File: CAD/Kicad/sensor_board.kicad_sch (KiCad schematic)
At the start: 3 parts, among them J2 RJ12_Shielded, U7 BME680, U8 MPU-9250

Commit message: It's super late man
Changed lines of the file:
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@@
+	)
+	(junction
+		(at 41.91 114.3)
+		(diameter 0)
+		(color 0 0 0 0)
 	)
 	(junction
@@
 	)
 	(junction
+		(at 58.42 106.68)
+		(diameter 0)
+		(color 0 0 0 0)
+	)
+	(junction
 		(at 109.22 149.86)
 		(diameter 0)
@@
 	(wire
 		(pts
-			(xy 52.07 106.68) (xy 106.68 106.68)
+			(xy 52.07 106.68) (xy 58.42 106.68)
 		)
 		(stroke
@@
 	(wire
 		(pts
+			(xy 58.42 106.68) (xy 106.68 106.68)
+		)
+		(stroke
+			(width 0)
+			(type default)
+		)
+	)
+	(wire
+		(pts
 			(xy 134.62 97.79) (xy 139.7 97.79)
 		)
@@
 	(wire
 		(pts
+			(xy 41.91 114.3) (xy 41.91 111.76)
+		)
+		(stroke
+			(width 0)
+			(type default)
+		)
+	)
+	(wire
+		(pts
 			(xy 102.87 40.64) (xy 95.25 40.64)
 		)
@@
 	(wire
 		(pts
-			(xy 41.91 149.86) (xy 41.91 111.76)
+			(xy 41.91 149.86) (xy 41.91 114.3)
 		)
 		(stroke
@@
 	(wire
 		(pts
+			(xy 58.42 114.3) (xy 58.42 106.68)
+		)
+		(stroke
+			(width 0)
+			(type default)
+		)
+	)
+	(wire
+		(pts
 			(xy 116.84 78.74) (xy 116.84 85.09)
 		)
 		(stroke
+			(width 0)
+			(type default)
+		)
+	)
+	(wire
+		(pts
+			(xy 41.91 114.3) (xy 58.42 114.3)
+		)
+		(stroke

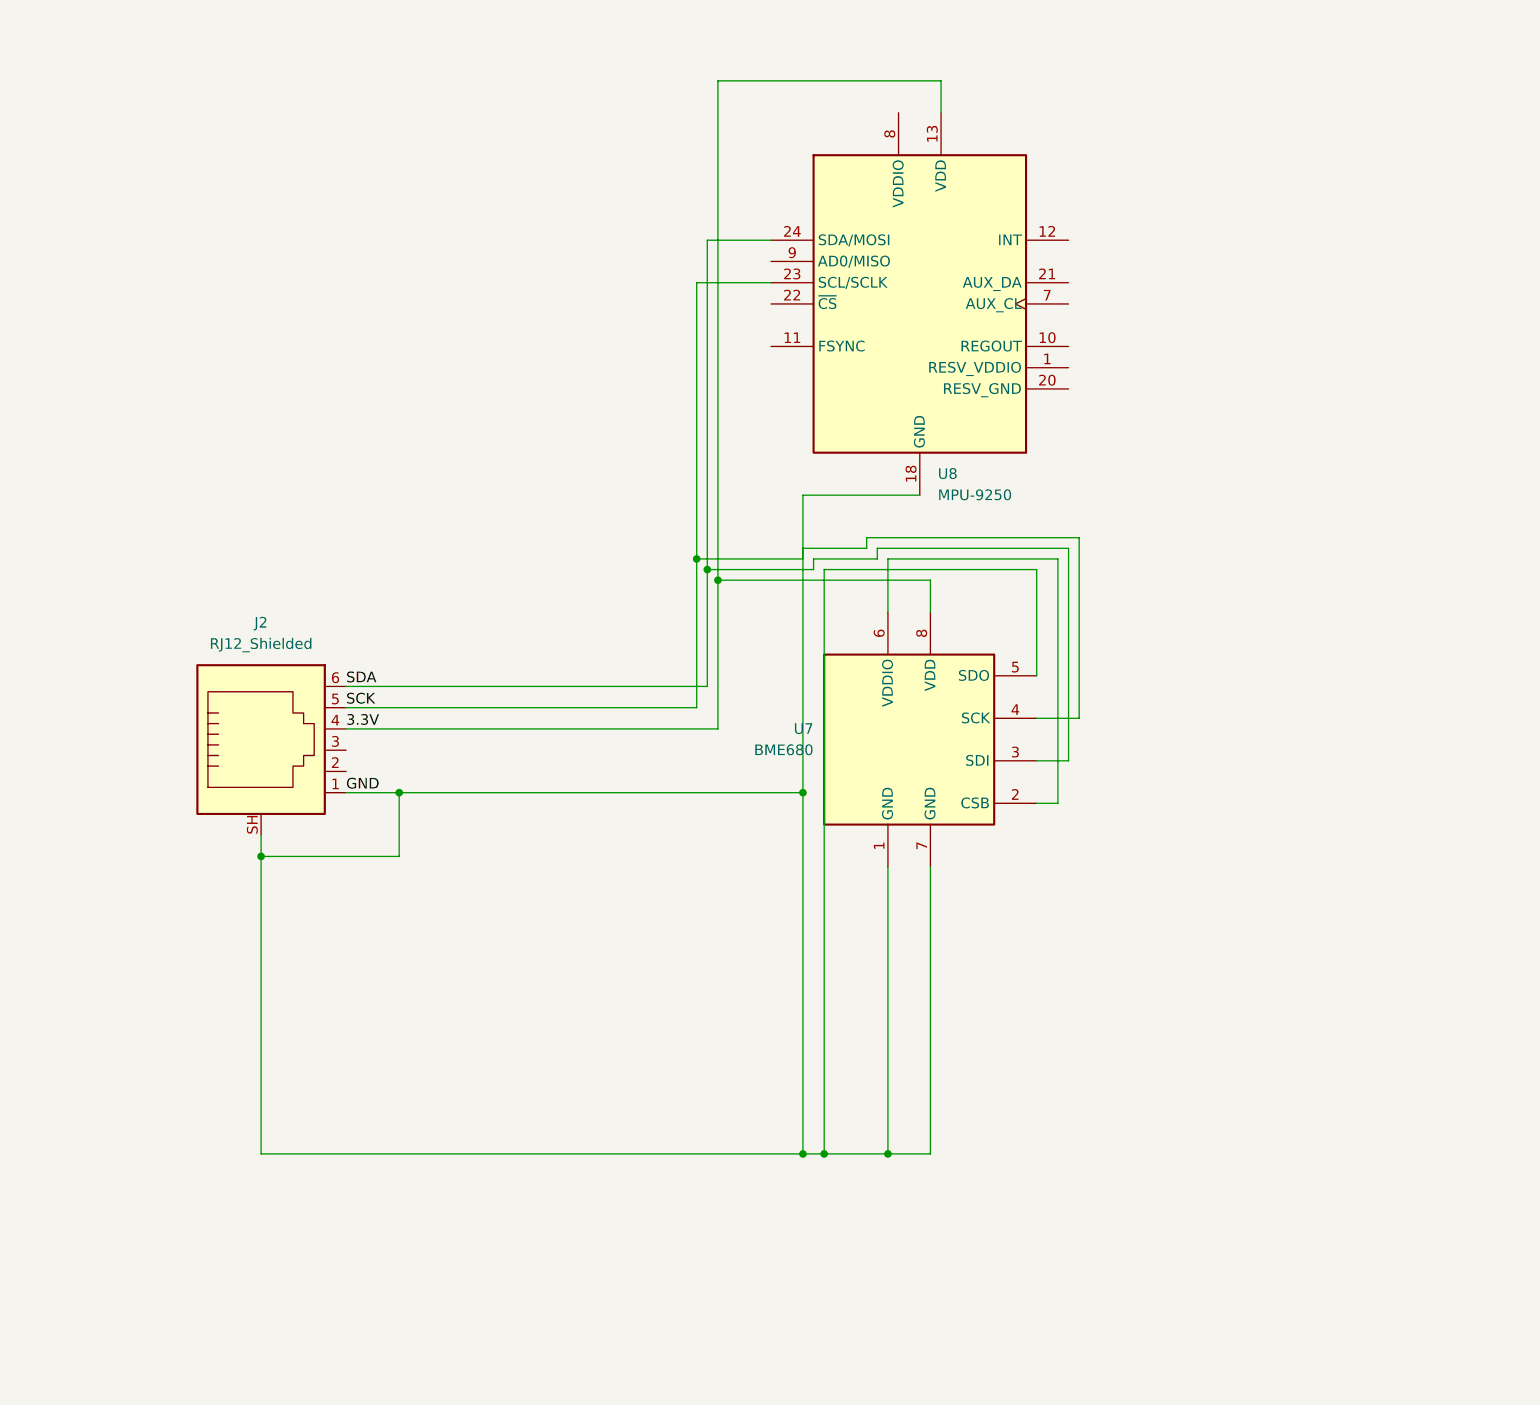
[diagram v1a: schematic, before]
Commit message: revised sensor board and redid I2C connections to both MCUs
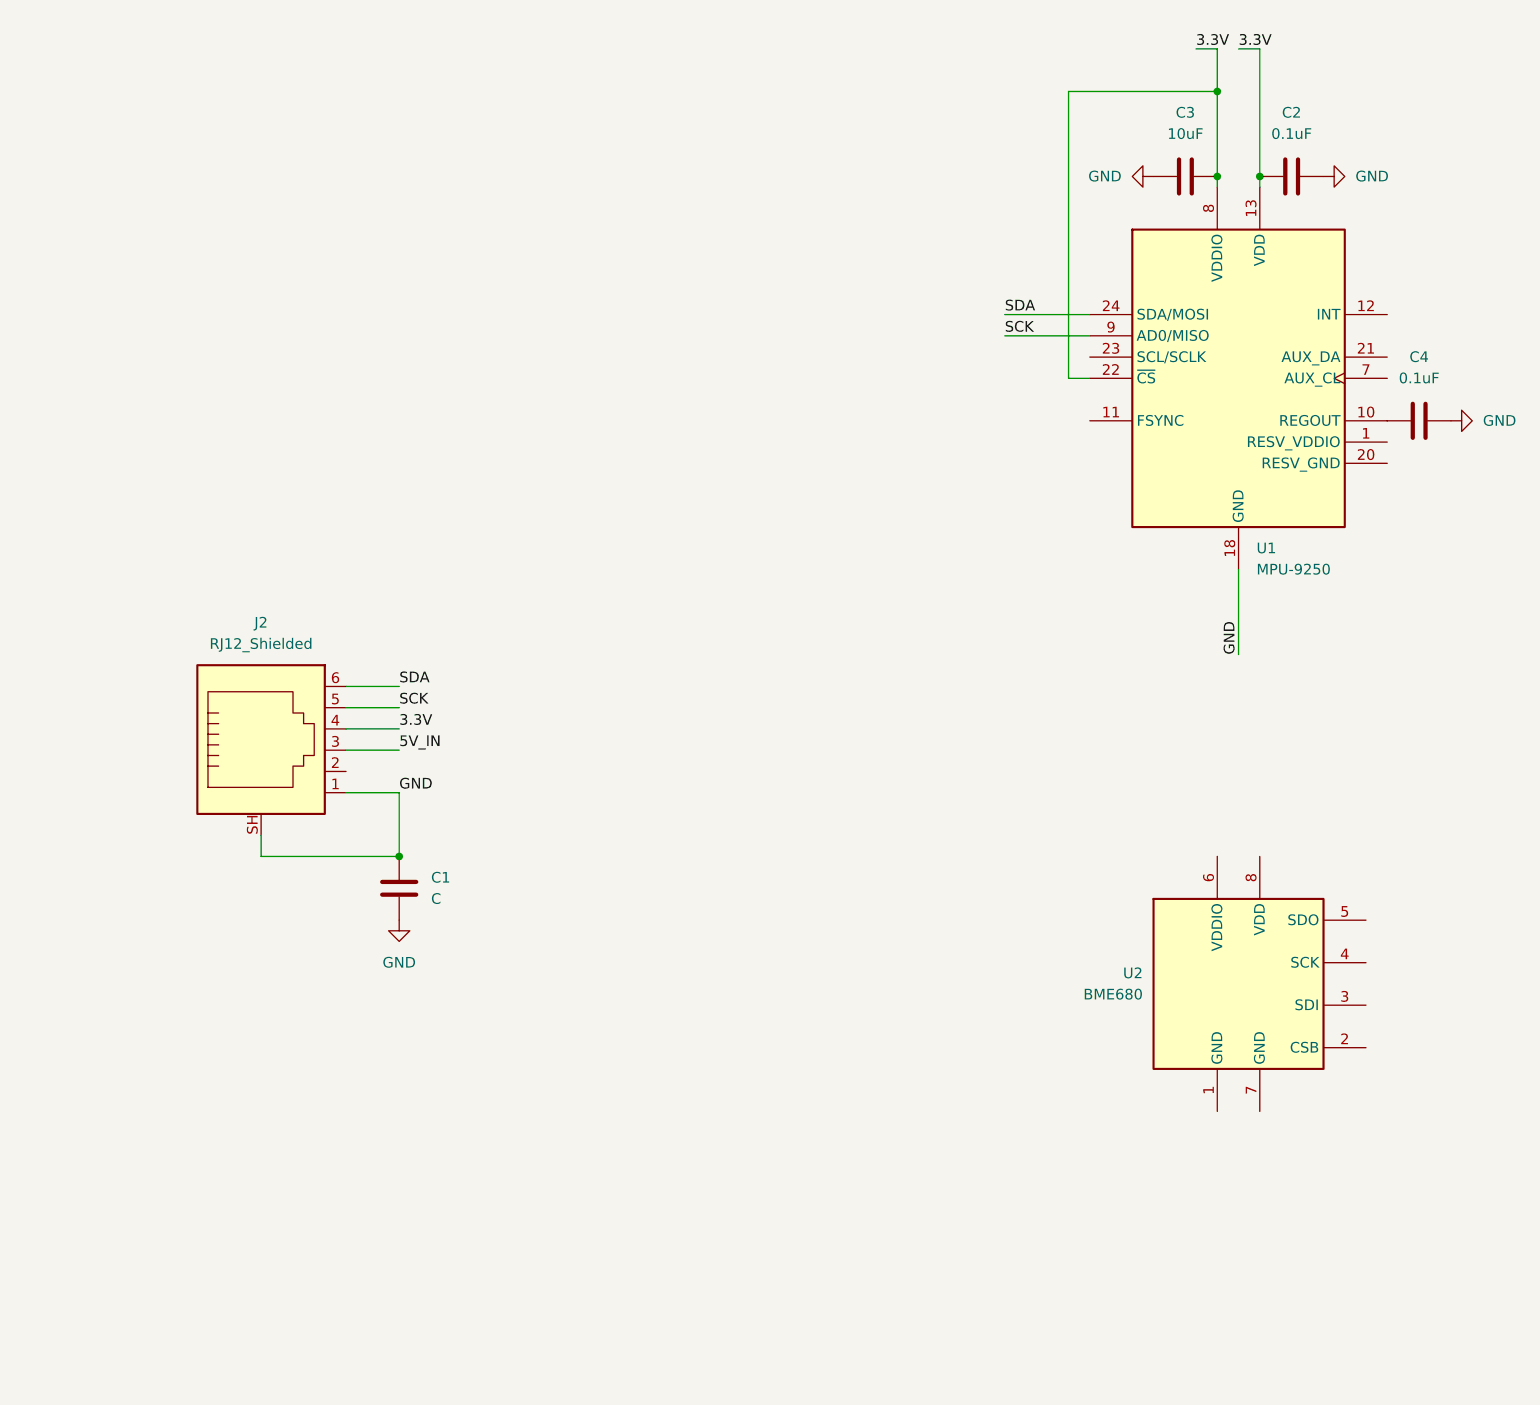
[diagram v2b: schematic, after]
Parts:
- removed U7: BME680, Package_LGA:Bosch_LGA-8_3x3mm_P0.8mm_ClockwisePinNumbering, symbol Sensor:BME680
- removed U8: MPU-9250, Sensor_Motion:InvenSense_QFN-24_3x3mm_P0.4mm, symbol Sensor_Motion:MPU-9250
- added C1: C, symbol Device:C
- added C2, C4: 0.1uF, symbol Device:C
- added C3: 10uF, symbol Device:C
- added U1: MPU-9250, Sensor_Motion:InvenSense_QFN-24_3x3mm_P0.4mm, symbol Sensor_Motion:MPU-9250
- added U2: BME680, Package_LGA:Bosch_LGA-8_3x3mm_P0.8mm_ClockwisePinNumbering, symbol Sensor:BME680
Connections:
- net 3.3V: now also C2.1, C3.2, U1.13 (VDD), U1.22 (~{CS}), U1.8 (VDDIO)
- net GND: now also C1.1, C1.2, C2.2, C3.1, C4.2, U1.18 (GND)
- net SCK: now also U1.9 (AD0/MISO)
- net SDA: now also U1.24 (SDA/MOSI)
- net 5V_IN: now reaches J2.3
- new net: C4.1, U1.10 (REGOUT)

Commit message: sensing revisions
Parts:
- removed C1: C, symbol Device:C
- removed J2: RJ12_Shielded, symbol Connector:RJ12_Shielded
- added FB1: FerriteBead, symbol Device:FerriteBead
- added J1: RJ45_Shielded, symbol Connector:RJ45_Shielded
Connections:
- net 3.3V: now also U1.1 (RESV_VDDIO), U1.11 (FSYNC), U1.21 (AUX_DA), U1.7 (AUX_CL), U2.2 (CSB), U2.6 (VDDIO), U2.8 (VDD), J1.4
- net 5V_IN: now also J1.3
- net GND: now also U1.20 (RESV_GND), U2.1 (GND), U2.5 (SDO), U2.7 (GND), FB1.1, FB1.2, J1.1, J1.SH
- net SCK: now also U1.23 (SCL/SCLK), U2.4 (SCK), J1.5; no longer U1.9 (AD0/MISO)
- net SDA: now also U2.3 (SDI), J1.6
- net INT: now reaches U1.12 (INT)
- net INT: now also J1.2
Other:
- note added: "Basic sesing board"
- moved on the sheet: C2, C3, C4, U1, U2

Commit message: Journal entry and small PCB tweaks
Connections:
- net GND: no longer FB1.1, J1.1, J1.SH
- net MOSI: now reaches J1.7
- net MISO: now reaches J1.8
- new net: FB1.1, J1.SH
- new net MCLCK: J1.1
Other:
- note added: "Basic sensing board"
- note removed: "Basic sesing board"
- moved on the sheet: C2, C3, C4, FB1, J1, U1, U2
